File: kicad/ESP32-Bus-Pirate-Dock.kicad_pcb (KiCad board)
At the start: 4 copper layers, 80 x 73.8 mm, 35 parts, among them CN1 HX25418-10WA, J1 Conn_01x10V, J2 Conn_01x22, J3 Conn_01x22, J4 Conn_02x03, J5 Conn_01x22, J6 Conn_01x22, J7 Conn_01x22, Q1 2N7002, U2 LDL1117S33R, U3 TMUX1574PW, U7 TMUX1574PW, U8 TXS0108EPW, U9 TXS0108EPW

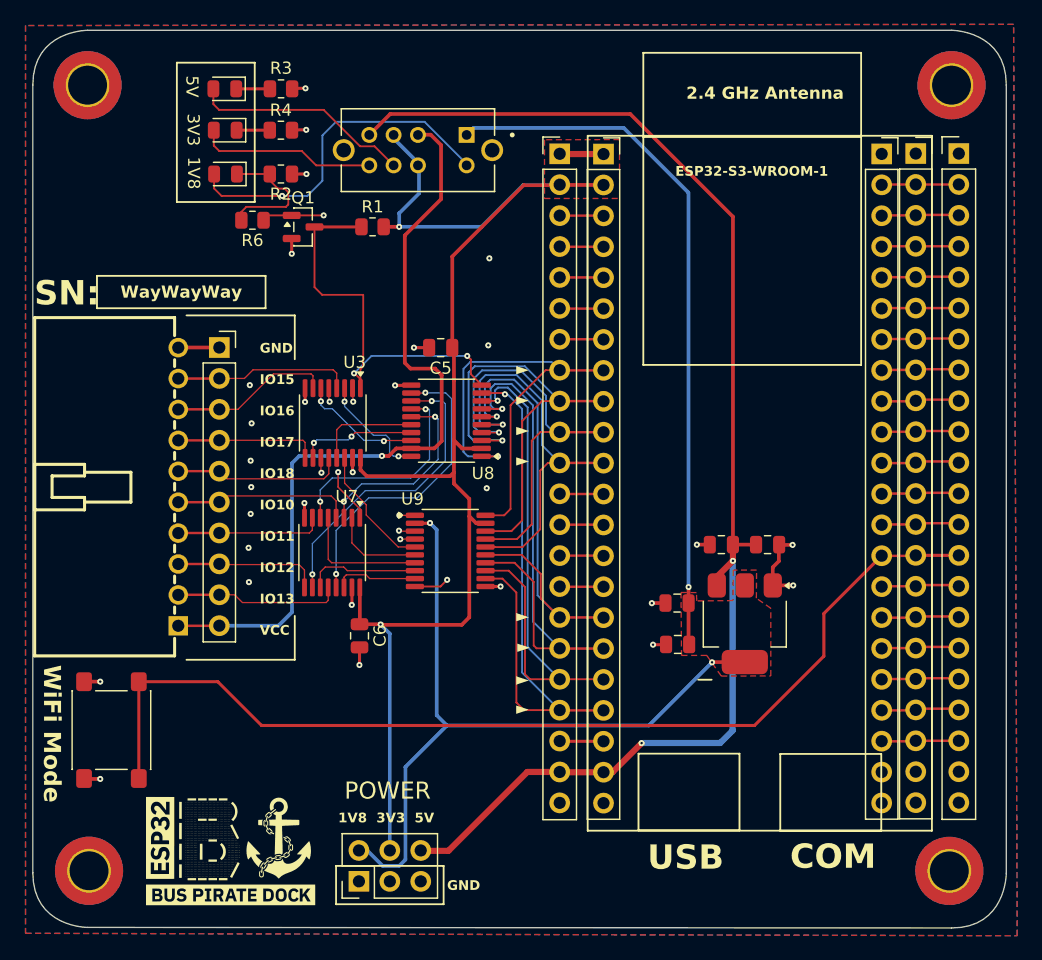
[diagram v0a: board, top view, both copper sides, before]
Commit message: Changed track widths  to 1.524mm
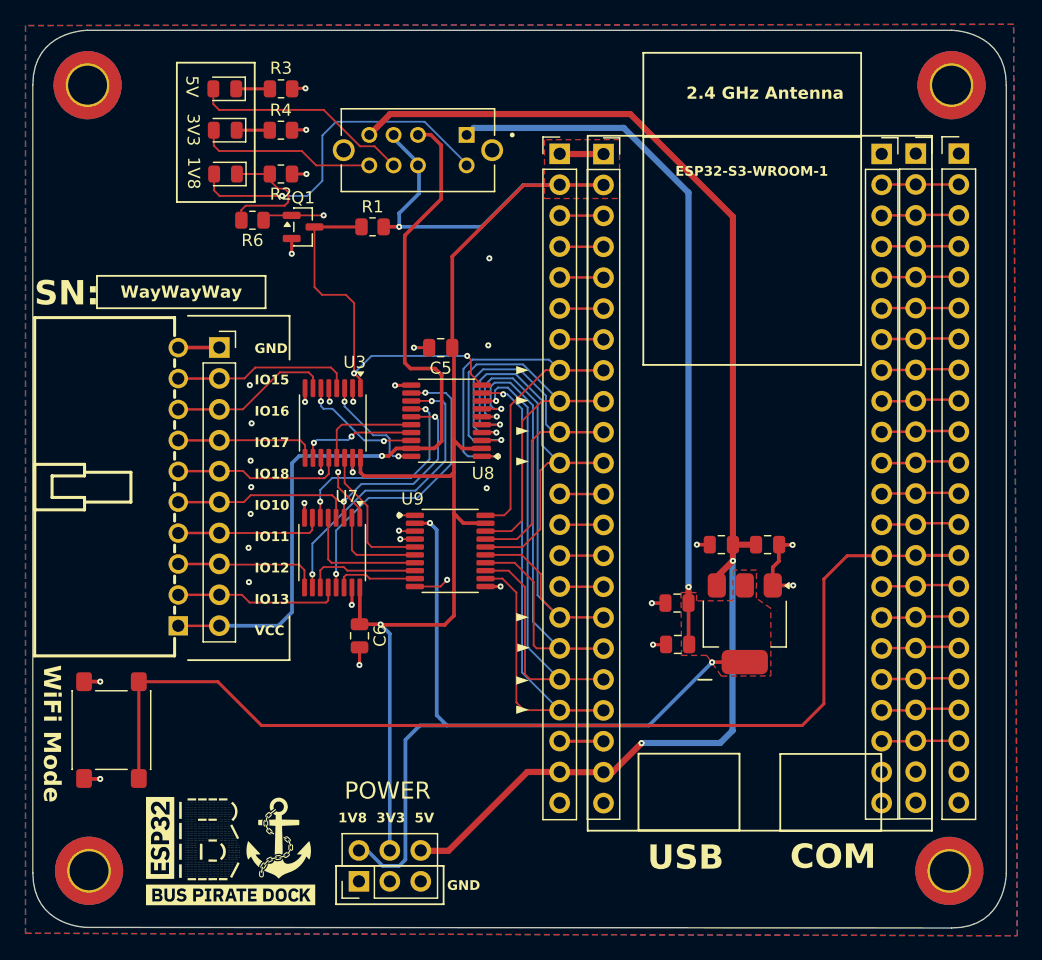
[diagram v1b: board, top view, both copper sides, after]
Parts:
- R6: value 100k -> 10k
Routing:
- net GPIO0: track 84.7 -> 88.6 mm
- net +1V8: track 119.8 -> 121.1 mm
- net /Voltage Level Translator/IO18_L: track 10.9 -> 12.2 mm
- net /Voltage Level Translator/SEL: track 50.9 -> 49.9 mm

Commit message: Changed DP3T switch
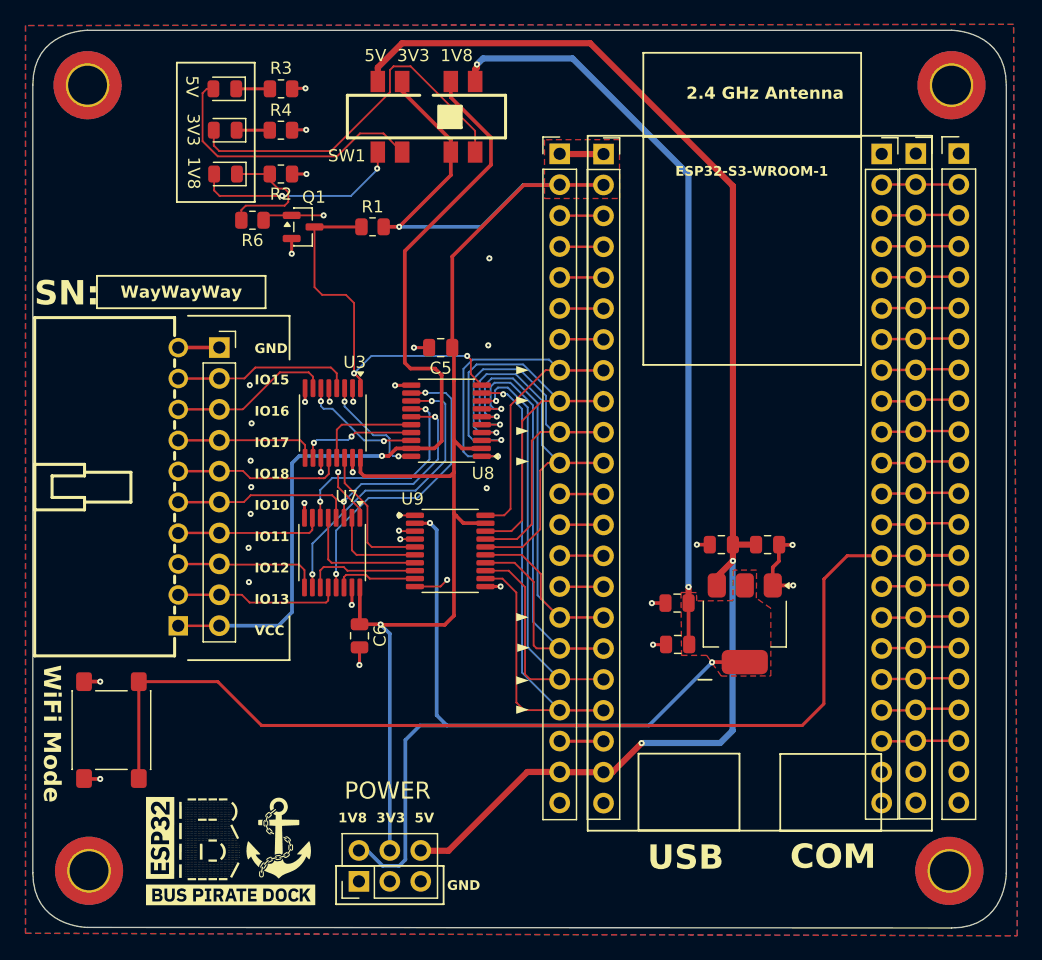
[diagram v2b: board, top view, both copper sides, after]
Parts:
- removed S1: EG2310, EG2310:SW_EG2310
- added SW1: TA-3532S-A2, TA-3532S-A2:SW-SMD_8P-L13.0-W3.5-P2.00, F.Cu at (156.1, 67.4)
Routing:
- net /Voltage Level Translator/D3_A: track 14.7 -> 30.8 mm
- net /Voltage Level Translator/D1_A: track 28.5 -> 17.3 mm, vias 1 -> 2
- net +3.3V: track 117.8 -> 124.0 mm
- net VTARGET: track 65.4 -> 71.4 mm
- net /Voltage Level Translator/D2_A: track 18.2 -> 23.3 mm
- net +5V: track 111.0 -> 115.5 mm
- net +1V8: track 121.1 -> 125.0 mm, vias 3 -> 4
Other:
- board text added: "5V 3V3 1V8"

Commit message: Modified PCB
- Added Keepout rule for Devkit Antenna
- Moved clone devkit header 0.2mm to better fit
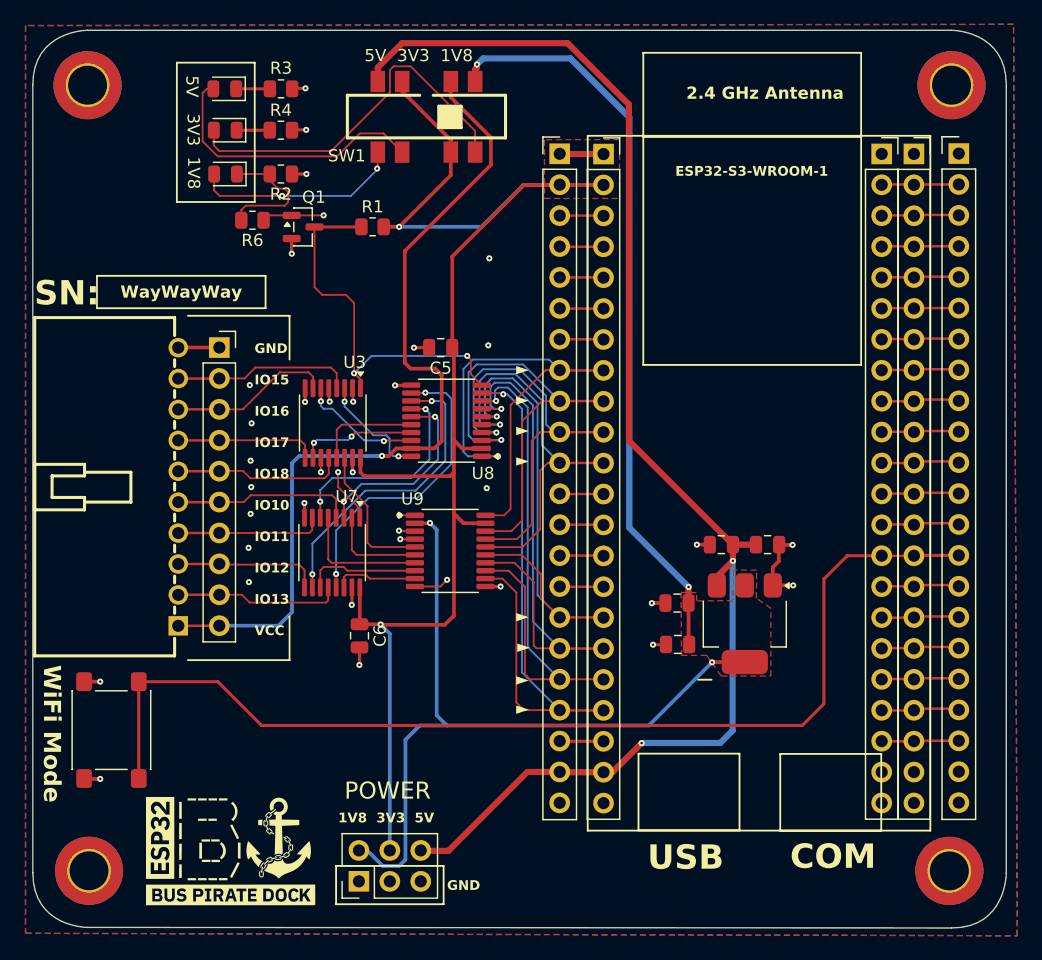
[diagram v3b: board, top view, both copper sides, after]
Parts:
- moved J5 0.15 mm to (196.1, 70.5)
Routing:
- net +5V: track 115.5 -> 114.4 mm

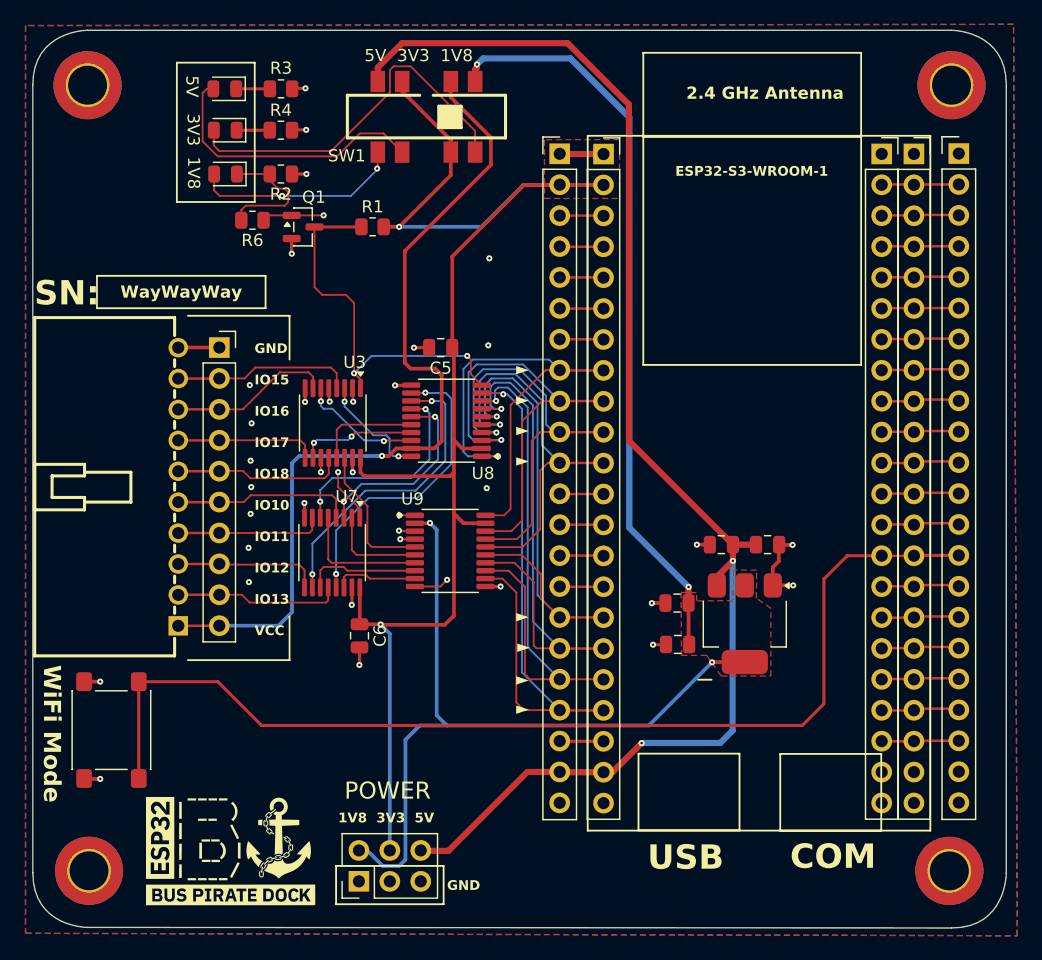
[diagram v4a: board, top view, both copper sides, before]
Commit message: New components PCB placement
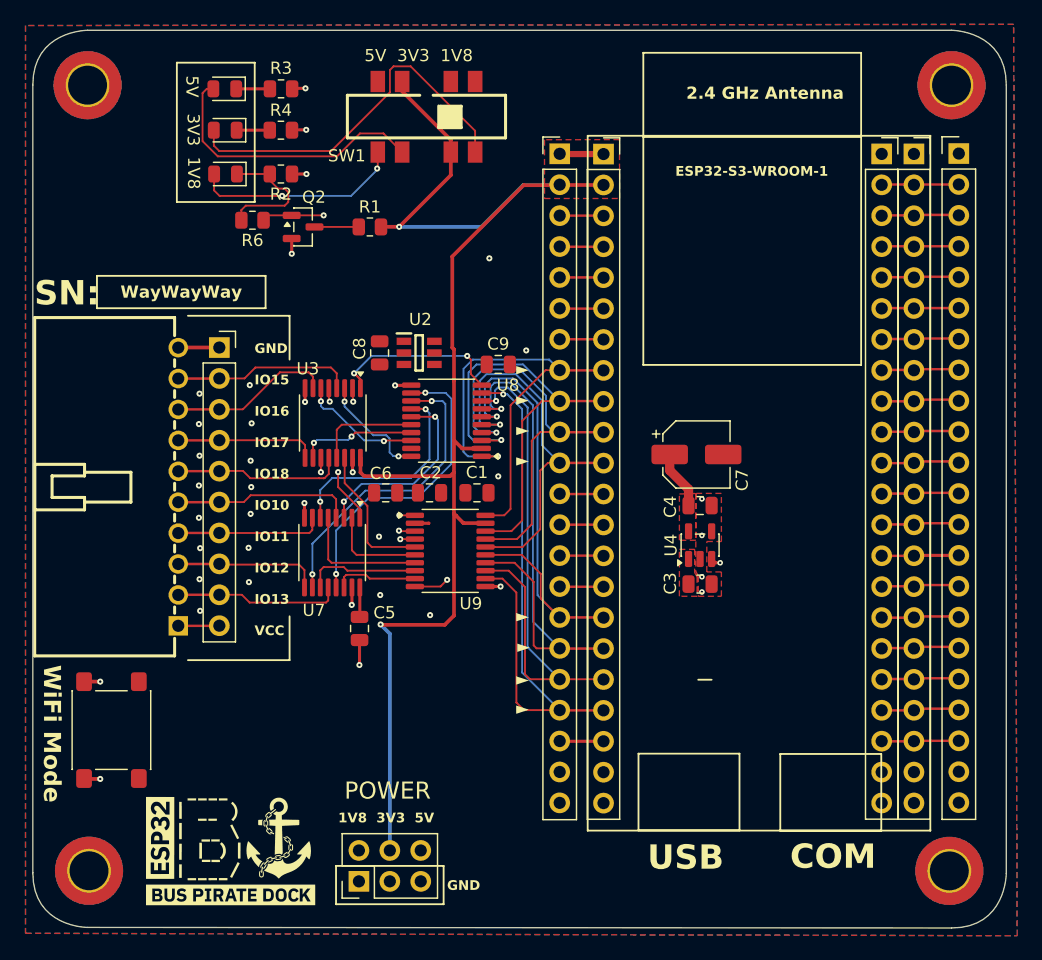
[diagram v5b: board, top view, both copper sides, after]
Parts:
- added C7: 22u, Capacitor_SMD:CP_Elec_5x4.5, F.Cu at (178.2, 95.2)
- added C8: 0.1u, Capacitor_SMD:C_0805_2012Metric, F.Cu at (152.2, 86.8)
- added C9: 0.1u, Capacitor_SMD:C_0805_2012Metric, F.Cu at (161.9, 87.8)
- added U4: TLV75518PDBV, Package_TO_SOT_SMD:SOT-23-5, F.Cu at (178.5, 102.6)
- C1, C2: value 4.7u -> 0.1u
- C3, C4: value 0.1u -> 1u
- C5, C6: value 0.1u -> 4.7u
- R2: value 1k -> 10k
- R6: value 10k -> 1k
- U2: value LDL1117S33R -> TS5A3157DBVR; footprint Package_TO_SOT_SMD:SOT-223-3_TabPin2 -> TS5A3157:SOT95P280X145-6N
- moved U2 34.8 mm to (155.4, 86.8), turned to 0 degrees
- moved C5 24.0 mm to (150.6, 109.5), turned to -90 degrees
- moved C2 23.9 mm to (156.3, 98.3)
- moved C1 20.5 mm to (160.2, 98.3), turned to 0 degrees
- moved C6 11.9 mm to (152.7, 98.3), turned to 0 degrees
- moved C4 8.23 mm to (178.5, 99.3), turned to 0 degrees
- moved C3 6.42 mm to (178.5, 105.8)
- moved R1 0.22 mm to (151.4, 76.5)
- renumbered Q1 to Q2
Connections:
- C1 pad 1: +5V -> +3.3V
- D1 pad 2: /Voltage Level Translator/D1_A -> +3.3V
- D2 pad 2: /Voltage Level Translator/D2_A -> +3.3V
- D3 pad 2: /Voltage Level Translator/D3_A -> +3.3V
- Q2 pad 1: /Voltage Level Translator/GATE -> /Voltage Level Translator/SEL
- Q2 pad 3: /Voltage Level Translator/SEL -> /Voltage Level Translator/~{SEL}
- R1 pad 1: /Voltage Level Translator/SEL -> /Voltage Level Translator/~{SEL}
- R2 pad 1: GND -> /Voltage Level Translator/SEL
- R2 pad 2: /Voltage Level Translator/D1_K -> +3.3V
- R3 pad 2: GND -> /Voltage Level Translator/3V3_SEL
- R4 pad 2: GND -> /Voltage Level Translator/5V_SEL
- R6 pad 1: /Voltage Level Translator/GATE -> /Voltage Level Translator/SEL
- SW1 pad 5: /Voltage Level Translator/D1_A -> /Voltage Level Translator/5V_SEL
- SW1 pad 6: /Voltage Level Translator/D2_A -> /Voltage Level Translator/3V3_SEL
- SW1 pad 7: +3.3V -> GND
- SW1 pad 8: /Voltage Level Translator/D3_A -> /Voltage Level Translator/SEL
- U2 pad 1: GND -> +3.3V
- U2 pad 2: +1V8 -> GND
- U2 pad 3: +5V -> VTARGET
- U8 pad 19: VTARGET -> /Voltage Level Translator/V_{ccB}_H
- U9 pad 10: /Voltage Level Translator/GATE -> /Voltage Level Translator/~{SEL}
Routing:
- net +1V8: track 124.9 -> 6.00 mm, vias 4 -> 0
- net +5V: track 114.4 -> 0.00 mm, vias 2 -> 0
- net GPIO0: track 88.6 -> 6.36 mm
- net VTARGET: track 71.4 -> 3.38 mm, vias 1 -> 0
- net /Voltage Level Translator/GATE: track 42.9 -> 0.00 mm, vias 2 -> 0
- net +3.3V: track 124.0 -> 162.2 mm, vias 2 -> 4
- net /Voltage Level Translator/D3_A: track 30.8 -> 0.00 mm
- net (no net): track 0.00 -> 30.8 mm
- net /Voltage Level Translator/SEL: track 49.9 -> 75.5 mm, vias 3 -> 6
- net /Voltage Level Translator/D2_A: track 23.3 -> 0.00 mm
- net /Voltage Level Translator/D1_A: track 17.3 -> 0.00 mm, vias 2 -> 0
- net GND: track 30.7 -> 16.8 mm, vias 29 -> 35
- net /Voltage Level Translator/~{SEL}: track 0.00 -> 3.64 mm
- net /Voltage Level Translator/3V3_SEL: track 0.00 -> 1.20 mm, vias 0 -> 1
- net /Voltage Level Translator/5V_SEL: track 0.00 -> 1.20 mm, vias 0 -> 1
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- added copper zone on F.Cu, net +5V

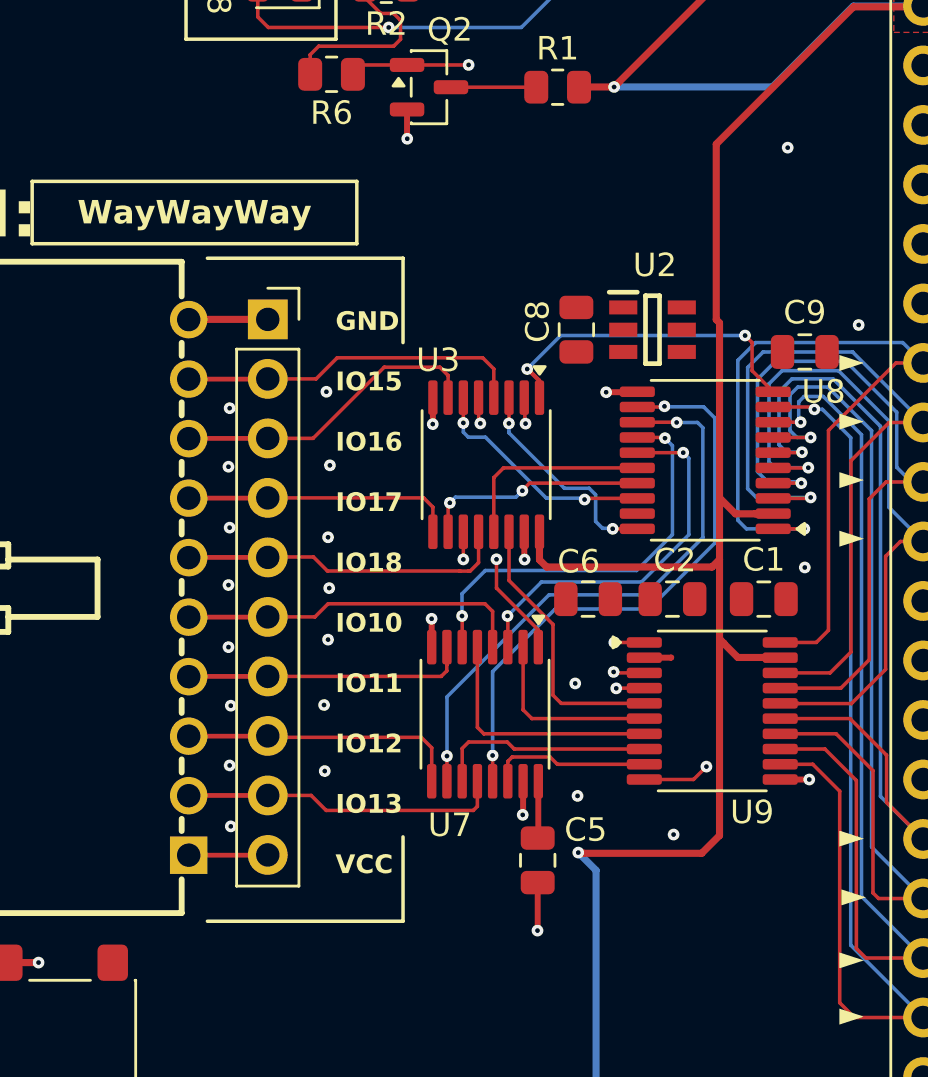
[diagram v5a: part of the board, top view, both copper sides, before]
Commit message: Updated PCB placement
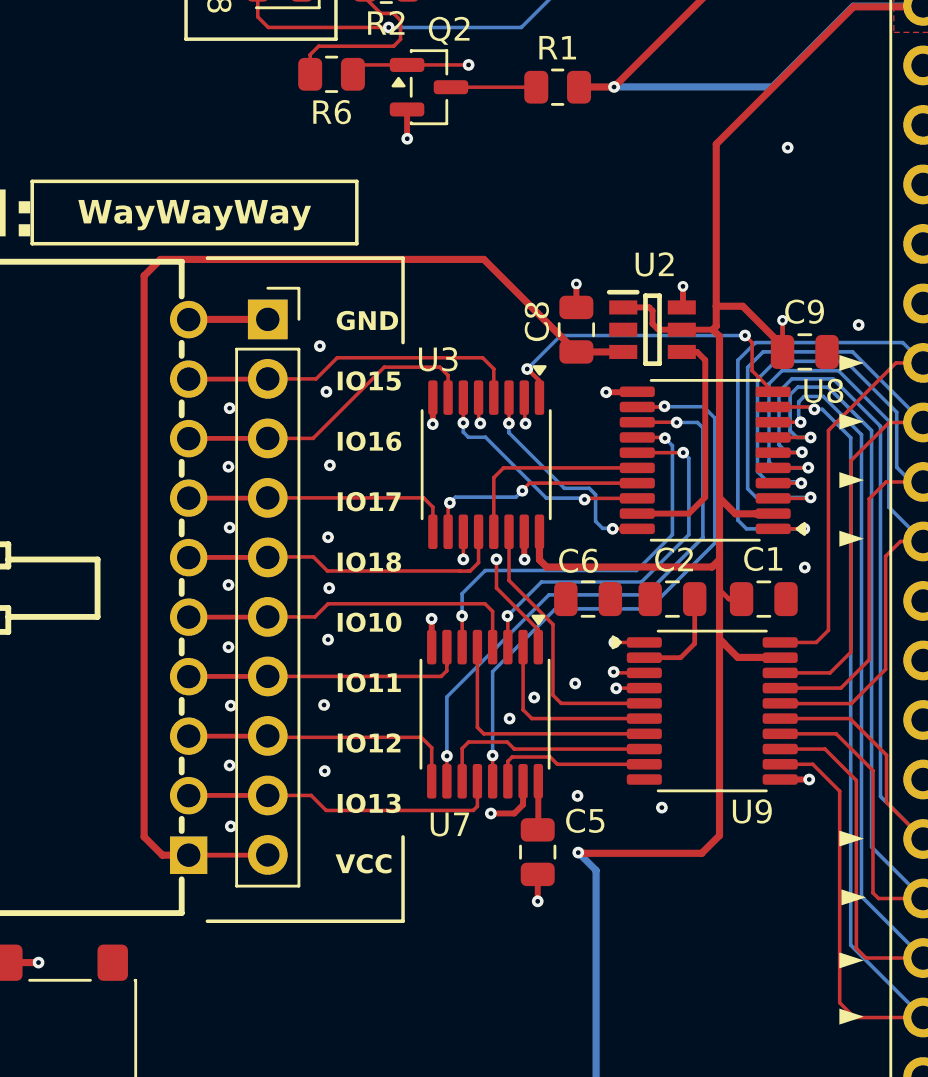
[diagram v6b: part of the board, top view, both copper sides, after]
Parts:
- moved C5 0.35 mm to (150.6, 109.1)
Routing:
- net VTARGET: track 3.38 -> 51.9 mm
- net /Voltage Level Translator/SEL: track 75.5 -> 57.1 mm
- net +3.3V: track 162.2 -> 173.1 mm, vias 4 -> 5
- net /Voltage Level Translator/V_{ccB}_H: track 0.00 -> 10.2 mm
- net +1V8: track 6.00 -> 9.14 mm
- net GND: track 16.8 -> 17.6 mm, vias 35 -> 39
